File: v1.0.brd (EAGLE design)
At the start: 160 x 100 mm, 19 parts, among them J1 DC-044-A, Q1 IRF520NPBF, U1 MCP23017-E/SO, U2 LM2599T-5.0, U3 74HC139N

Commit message: ADC
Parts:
- added U$1, U$2: MCP3424-E/SL, MCP3424:SOIC127P600X175-14N
- moved C4 2.84 mm to (-142.2, -194.3)
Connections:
- new net N$10: U$1.9
- new net N$11: U$1.10
- new net N$12: U$1.1
- new net N$13: U$1.2
- new net N$14: U$1.3
- new net N$15: U$1.4
- new net N$16: U$1.11
- new net N$8: U$2.9
- new net N$9: U$2.10
- new net VDD: U$1.6, U$2.6
- new net VSS: U$1.5, U$2.5
- net SCL_3V3: now also U$1.8, U$2.8
- net SDA_3V3: now also U$1.7, U$2.7
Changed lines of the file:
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@@
 <attribute name="MPN" value="SS54B" x="-151.13" y="-182.88" size="1.778" layer="27" display="off"/>
 </element>
-<element name="C4" library="Seeed-OPL-2017-01-Capacitor-akita" package="CAP_TH_P35_D80_POL" value="CAP_TH_220UF_25V" x="-144.78" y="-195.58"/>
+<element name="C4" library="Seeed-OPL-2017-01-Capacitor-akita" package="CAP_TH_P35_D80_POL" value="CAP_TH_220UF_25V" x="-142.24" y="-194.31"/>
 <element name="L1" library="inductors" library_urn="urn:adsk.eagle:library:243" package="DR125" value="DR125-330-R 33uH" x="-162.56" y="-193.04"/>
 <element name="USB1" library="Seeed-Connector -2016" package="MICRO-USB5+4P-SMD-0.65-B" value="ST-USB-001G" x="-160.02" y="-205.74">
@@
 <element name="R4" library="Seeed-Resistor-2016" package="R0603" value="100K" x="-181.61" y="-217.17">
 <attribute name="MPN" value="RC0603FR-07100KL" x="-181.61" y="-217.17" size="1.778" layer="27" display="off"/>
+</element>
+<element name="U$1" library="MCP3424" package="SOIC127P600X175-14N" value="MCP3424-E/SL" x="-191.77" y="-212.09">
+<attribute name="MPN" value="MCP3424-E/SL" x="-191.77" y="-212.09" size="1.778" layer="27" display="off"/>
+<attribute name="OC_FARNELL" value="1630424" x="-191.77" y="-212.09" size="1.778" layer="27" display="off"/>
+<attribute name="OC_NEWARK" value="54M4871" x="-191.77" y="-212.09" size="1.778" layer="27" display="off"/>
+<attribute name="PACKAGE" value="SOIC-14" x="-191.77" y="-212.09" size="1.778" layer="27" display="off"/>
+<attribute name="SUPPLIER" value="Microchip" x="-191.77" y="-212.09" size="1.778" layer="27" display="off"/>
+</element>
+<element name="U$2" library="MCP3424" package="SOIC127P600X175-14N" value="MCP3424-E/SL" x="-205.74" y="-212.09">
+<attribute name="MPN" value="MCP3424-E/SL" x="-205.74" y="-212.09" size="1.778" layer="27" display="off"/>
+<attribute name="OC_FARNELL" value="1630424" x="-205.74" y="-212.09" size="1.778" layer="27" display="off"/>
+<attribute name="OC_NEWARK" value="54M4871" x="-205.74" y="-212.09" size="1.778" layer="27" display="off"/>
+<attribute name="PACKAGE" value="SOIC-14" x="-205.74" y="-212.09" size="1.778" layer="27" display="off"/>
+<attribute name="SUPPLIER" value="Microchip" x="-205.74" y="-212.09" size="1.778" layer="27" display="off"/>
 </element>
 </elements>
@@
 <contactref element="U1" pad="12"/>
 <contactref element="PCB1" pad="P$5"/>
+<contactref element="U$1" pad="8"/>
+<contactref element="U$2" pad="8"/>
+<wire x1="-189.4078" y1="-215.9" x2="-203.3778" y2="-215.9" width="0" layer="19" extent="1-1"/>
+<wire x1="-121.3612" y1="24.765" x2="-189.4078" y2="-215.9" width="0" layer="19" extent="1-1"/>
 <wire x1="5.9182" y1="69.1134" x2="-121.3612" y2="24.765" width="0" layer="19" extent="1-1"/>
 </signal>
@@
 <contactref element="U1" pad="13"/>
 <contactref element="PCB1" pad="P$3"/>
+<contactref element="U$1" pad="7"/>
+<contactref element="U$2" pad="7"/>
+<wire x1="-194.1322" y1="-215.9" x2="-208.1022" y2="-215.9" width="0" layer="19" extent="1-1"/>
+<wire x1="-121.3612" y1="23.495" x2="-194.1322" y2="-215.9" width="0" layer="19" extent="1-1"/>
 <wire x1="5.9182" y1="71.6534" x2="-121.3612" y2="23.495" width="0" layer="19" extent="1-1"/>
 </signal>
@@
 <contactref element="R2" pad="1"/>
 <wire x1="-134.62" y1="-181.1475" x2="-87.63" y2="-151.13" width="0" layer="19" extent="1-1"/>
-<wire x1="-143.03" y1="-195.58" x2="-134.62" y2="-181.1475" width="0" layer="19" extent="1-1"/>
-<wire x1="-157.585" y1="-193.04" x2="-143.03" y2="-195.58" width="0" layer="19" extent="1-1"/>
+<wire x1="-140.49" y1="-194.31" x2="-134.62" y2="-181.1475" width="0" layer="19" extent="1-1"/>
+<wire x1="-157.585" y1="-193.04" x2="-140.49" y2="-194.31" width="0" layer="19" extent="1-1"/>
 <wire x1="-171.45" y1="-209.0875" x2="-157.585" y2="-193.04" width="0" layer="19" extent="1-1"/>
 <wire x1="-107.95" y1="-60.7314" x2="-87.63" y2="-151.13" width="0" layer="19" extent="1-1"/>
@@
 <wire x1="-144.78" y1="-184.912" x2="-139.7" y2="-184.912" width="0" layer="19" extent="1-1"/>
 <wire x1="-153.34" y1="-182.88" x2="-144.78" y2="-184.912" width="0" layer="19" extent="1-1"/>
-<wire x1="-146.53" y1="-195.58" x2="-144.78" y2="-184.912" width="0" layer="19" extent="1-1"/>
-<wire x1="-156.62" y1="-206.167" x2="-146.53" y2="-195.58" width="0" layer="19" extent="1-1"/>
+<wire x1="-143.99" y1="-194.31" x2="-144.78" y2="-184.912" width="0" layer="19" extent="1-1"/>
+<wire x1="-156.62" y1="-206.167" x2="-143.99" y2="-194.31" width="0" layer="19" extent="1-1"/>
 <wire x1="-158.72" y1="-205.99" x2="-156.62" y2="-206.167" width="0" layer="19" extent="1-1"/>
 <wire x1="-156.7942" y1="-208.915" x2="-156.62" y2="-206.167" width="0" layer="19" extent="1-1"/>
@@
 <wire x1="-159.37" y1="-205.99" x2="-181.61" y2="-216.408" width="0" layer="19" extent="1-1"/>
 </signal>
+<signal name="VDD">
+<contactref element="U$1" pad="6"/>
+<contactref element="U$2" pad="6"/>
+<wire x1="-194.1322" y1="-214.63" x2="-208.1022" y2="-214.63" width="0" layer="19" extent="1-1"/>
+</signal>
+<signal name="VSS">
+<contactref element="U$1" pad="5"/>
+<contactref element="U$2" pad="5"/>
+<wire x1="-194.1322" y1="-213.36" x2="-208.1022" y2="-213.36" width="0" layer="19" extent="1-1"/>
+</signal>
+<signal name="N$8">
+<contactref element="U$2" pad="9"/>
+</signal>
+<signal name="N$9">
+<contactref element="U$2" pad="10"/>
+</signal>
+<signal name="N$10">
+<contactref element="U$1" pad="9"/>
+</signal>
+<signal name="N$11">
+<contactref element="U$1" pad="10"/>
+</signal>
+<signal name="N$12">
+<contactref element="U$1" pad="1"/>
+</signal>
+<signal name="N$13">
+<contactref element="U$1" pad="2"/>
+</signal>
+<signal name="N$14">
+<contactref element="U$1" pad="3"/>
+</signal>
+<signal name="N$15">
+<contactref element="U$1" pad="4"/>
+</signal>
+<signal name="N$16">
+<contactref element="U$1" pad="11"/>
+</signal>
 </signals>

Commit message: General tidying, PSU mods, and pycom library created and added
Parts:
- removed D3: GREEN-0603, Seeed-LED-2016:LED-0603
- removed Q1: IRF520NPBF, Seeed-Transistor-2016:TO-220
- removed R3: 1K, Seeed-Resistor-2016:R0603
- removed R4: 100K, Seeed-Resistor-2016:R0603
- removed U3: 74HC139N, 74HC139N:DIP254P762X420-16
- removed USB1: ST-USB-001G, Seeed-Connector -2016:MICRO-USB5+4P-SMD-0.65-B
- added C11, C12, C13, C14, C6, C7: 100nf, Seeed-Capacitor-2016:C0603
- added C5, C8: 1UF 6.3V, Seeed-Capacitor-2016:C0402
- added D10, D4, D5, D6, D7, D8, D9: RED-0603, Seeed-LED-2016:LED-0603
- added L2, L3: 330R-1500MA, Seeed-Inductor-2016:L0805
- added R10, R11, R5, R6, R7, R8, R9: 1K, Seeed-Resistor-2016:R0603
- added TP1: PTR1B2,54, testpad:B2,54
- added TP2, TP3: TPB2,54, testpad:B2,54
- added U$3: LOPY, pycom:LOPY
- added U10: 74HC139N, 74HC139N:DIP254P762X420-16
- added USB2: ST-USB-001G, Seeed-Connector -2016:MICRO-USB5+4P-SMD-0.65-B
- R2: value 10K 1/16W -> 100K; device Seeed-Resistor-2016:R0402 -> Seeed-Resistor-2016:R0603
- moved U$1 349.4 mm to (-27.9, 96.5)
- moved U$2 345.9 mm to (-49.5, 96.5)
- moved L1 325.5 mm to (-48.3, 111.8)
- moved C2 315.7 mm to (-62.2, 121.9)
- moved C3 315.7 mm to (-67.3, 121.9)
- moved C4 314.5 mm to (-69.8, 111.8)
- moved C1 306.8 mm to (-27.9, 113.0)
- moved R1 296.9 mm to (-88.9, 111.8)
- moved D2 295.3 mm to (-108.0, 109.2)
- moved D1 277.0 mm to (-100.3, 109.2)
- moved PCB1 176.1 mm to (-100.3, 3.81), flipped to the top, turned to 0 degrees
- moved J1 156.1 mm to (-92.7, 61.0)
- moved U2 134.6 mm to (-74.9, 76.2)
- moved R2 118.0 mm to (-154.9, -92.7)
- moved U1 81.5 mm to (-47.0, 72.4)
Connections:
- removed net N$10: U$1.9
- removed net N$11: U$1.10
- removed net N$5: R4.1, USB1.4
- removed net N$8: U$2.9
- removed net N$9: U$2.10
- removed net VDD: U$1.6, U$2.6
- removed net VSS: U$1.5, U$2.5
- new net +24V: C1.P$P, D1.-, R5.2, U2.1
- new net LOPY_3V3: U$3.P$26
- new net LOPY_P0: U$3.P$2
- new net LOPY_P1: U$3.P$3
- new net LOPY_P10: U$3.P$12
- new net LOPY_P11: U$3.P$13
- new net LOPY_P12: U$3.P$14
- new net LOPY_P13: U$3.P$15
- new net LOPY_P14: U$3.P$16
- new net LOPY_P15: U$3.P$17
- new net LOPY_P16: U$3.P$18
- new net LOPY_P17: U$3.P$19
- new net LOPY_P18: U$3.P$20
- new net LOPY_P19: U$3.P$21
- new net LOPY_P2: U$3.P$4
- new net LOPY_P20: U$3.P$22
- new net LOPY_P21: U$3.P$23
- new net LOPY_P22: U$3.P$24
- new net LOPY_P23: U$3.P$25
- new net LOPY_P3: U$3.P$5
- new net LOPY_P4: U$3.P$6
- new net LOPY_P8: U$3.P$10
- new net LOPY_P9: U$3.P$11
- new net LOPY_RST: U$3.P$1
- new net N$19: C5.1, C7.2, U$2.6
- new net N$22: C14.2, L2.2, TP3.TP
- new net N$23: D10.-, D4.-, D5.-, D6.-, D7.-, D8.-, D9.-
- new net N$28: D10.+, R11.1
- new net N$29: D9.+, R10.1
- new net N$30: D8.+, R9.1
- new net N$31: D7.+, R8.1
- new net N$32: D6.+, R7.1
- new net N$33: D5.+, R6.1
- new net N$34: D4.+, R5.1
- net +3V3: now also C11.2, C12.2, L2.1, TP2.TP
- net +5V: now also C13.2, R6.2, U$3.P$28, U10.16; no longer U3.16
- net +5V/1: now also USB2.1; no longer Q1.3, R3.1, USB1.1
- net +5V_REG_OUT: now also TP1.TP; no longer Q1.1, R2.1
- net GND: now also C1.P$M, C11.1, C12.1, C13.1, C2.2, C3.2, C4.P$P, D2.+, L3.1, U$3.P$27, U10.8, U2.4; no longer U3.8
- net GNDA: now also C14.1, C5.2, C7.1, L3.2, R2.2, U$1.10, U$1.5, U$1.9, U$2.5, U$2.9, USB2.5, USB2.S1, USB2.S2, USB2.S3, USB2.S4, USB2.S5, USB2.S6; no longer C1.P$M, C2.2, C3.2, C4.P$P, D2.+, D3.-, Q1.2, Q1.HEAT, R4.2, U2.4, USB1.5, USB1.S1, USB1.S2, USB1.S3, USB1.S4, USB1.S5, USB1.S6
- net N$1: now also R2.1, USB2.4; no longer D3.+, R3.2
- net N$12: now also C6.2, C8.1, U$1.6; no longer U$1.1
- net N$2: now also C6.1, C8.2; no longer C1.P$P, D1.-, U2.1
- net SPI0_CS0: now also U10.1; no longer U3.1
- net SPI0_CS1: now also U10.15; no longer U3.15

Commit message: seeed dc-dc library finished RTC added
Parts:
- removed C1: CAP_TH_470UF_50V, Seeed-OPL-2017-01-Capacitor-akita:CAP_TH_P50_D100_POL
- removed C3: 100nf, Seeed-Capacitor-2016:C0603
- removed C4: CAP_TH_220UF_25V, Seeed-OPL-2017-01-Capacitor-akita:CAP_TH_P35_D80_POL
- removed D2: 28V-5A, Seeed-Diode-2016:DO-214AA
- removed L1: DR125-330-R 33uH, inductors:DR125
- removed R1: 10K 1/16W, Seeed-Resistor-2016:R0402
- removed TP1: PTR1B2,54, testpad:B2,54
- added BAT1: cr1220, Seeed-Connector -2016:BAT2P-13.5-CR1220
- added TP4: TPB2,54, testpad:B2,54
- added U4: GROVE_DC&DC, seeed_parts:GROVE_DC&DC
- U2: value LM2599T-5.0 -> MCP79412-I/SN; device LM2599T:TO127P470X1016X1740-7P -> imported-parts:SOIC127P600X175-8N
- moved C2 344.2 mm to (-214.6, -186.7)
- moved U2 275.5 mm to (-200.7, -168.9)
- renumbered U$3 to U3
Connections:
- removed net +5V_REG_OUT: C4.P$M, L1.2, R1.1, TP1.TP, U2.6
- removed net N$4: D2.-, L1.1, U2.2
- removed net N$6: C3.1, U2.5
- removed net N$7: R1.2, U2.3
- new net 5V4: R7.2, TP4.TP, U4.P$5, U4.P$6
- net +24V: now also U4.P$1, U4.P$2; no longer C1.P$P, U2.1
- net +3V3: now also C2.2, U2.8
- net GND: now also BAT1.-, C2.1, J1.-, J1.CDN, U4.P$3, U4.P$4, U4.P$7, U4.P$8; no longer C1.P$M, C2.2, C3.2, C4.P$P, D2.+
- net GNDA: no longer J1.-, J1.CDN
- net N$3: now also BAT1.+1, BAT1.+2, U2.3; no longer C2.1, U2.7
- net SCL_3V3: now also U2.6
- net SDA_3V3: now also U2.5

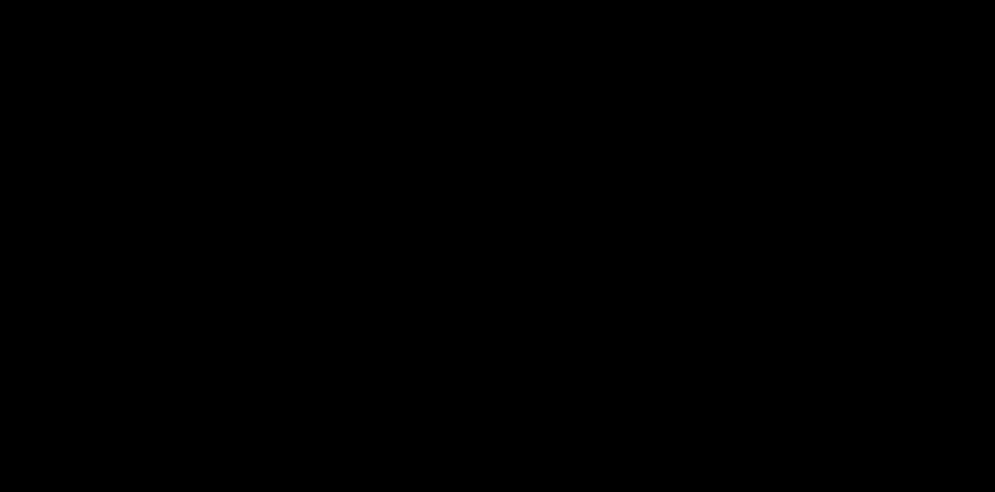
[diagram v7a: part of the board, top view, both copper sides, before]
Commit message: added crystal for RTC
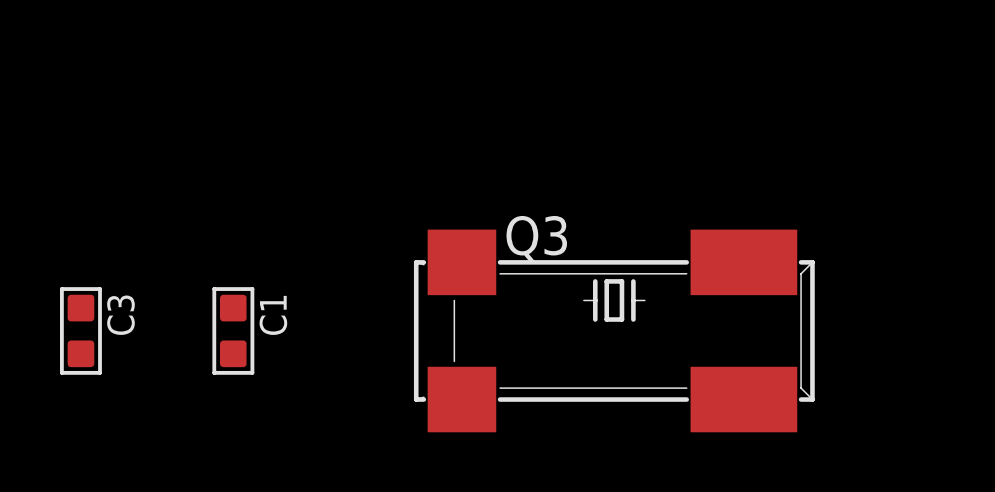
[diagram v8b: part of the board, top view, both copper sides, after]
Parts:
- added C1, C3: 100nf, Seeed-Capacitor:C0603
- added Q3: 6pF@32.7680kHz, crystal:86SMX
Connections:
- new net X1_RTC: C1.1, Q3.4, U2.1
- new net X2_RTC: C3.1, Q3.1, U2.2
- net GND: now also C1.2, C3.2
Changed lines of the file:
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@@
 <attribute name="MPN" value="CC0603KRX7R9BB104" x="-214.63" y="-186.69" size="1.778" layer="27" display="off"/>
+</element>
+<element name="Q3" library="crystal" package="86SMX" value="6pF@32.7680kHz" x="-207.01" y="-213.36"/>
+<element name="C1" library="Seeed-Capacitor" library_urn="urn:adsk.eagle:library:464" package="C0603" value="100nf" x="-219.71" y="-213.36">
+<attribute name="MPN" value="CC0603KRX7R9BB104" x="-219.71" y="-213.36" size="1.778" layer="27" display="off"/>
+</element>
+<element name="C3" library="Seeed-Capacitor" library_urn="urn:adsk.eagle:library:464" package="C0603" value="100nf" x="-224.79" y="-213.36">
+<attribute name="MPN" value="CC0603KRX7R9BB104" x="-224.79" y="-213.36" size="1.778" layer="27" display="off"/>
 </element>
 </elements>
@@
 <contactref element="C2" pad="1"/>
 <contactref element="BAT1" pad="-"/>
+<contactref element="C1" pad="2"/>
+<contactref element="C3" pad="2"/>
 <wire x1="-164.719" y1="-102.87" x2="-160.02" y2="-90.678" width="0" layer="19" extent="1-1"/>
 <wire x1="-148.59" y1="-68.58" x2="-160.02" y2="-90.678" width="0" layer="19" extent="1-1"/>
@@
 <wire x1="-196.85" y1="-182.88" x2="-203.0222" y2="-170.815" width="0" layer="19" extent="1-1"/>
 <wire x1="-214.63" y1="-185.928" x2="-196.85" y2="-182.88" width="0" layer="19" extent="1-1"/>
+<wire x1="-219.71" y1="-214.122" x2="-214.63" y2="-185.928" width="0" layer="19" extent="1-1"/>
+<wire x1="-224.79" y1="-214.122" x2="-219.71" y2="-214.122" width="0" layer="19" extent="1-1"/>
 <wire x1="-114.3" y1="4.572" x2="-129.54" y2="-43.688" width="0" layer="19" extent="1-1"/>
 <wire x1="-86.8934" y1="57.5818" x2="-114.3" y2="4.572" width="0" layer="19" extent="1-1"/>
@@
 <wire x1="-190.119" y1="-182.88" x2="-203.581" y2="-182.88" width="0" layer="19" extent="1-1"/>
 </signal>
+<signal name="X1_RTC">
+<contactref element="U2" pad="1"/>
+<contactref element="Q3" pad="4"/>
+<contactref element="C1" pad="1"/>
+<wire x1="-212.09" y1="-211.074" x2="-219.71" y2="-212.598" width="0" layer="19" extent="1-1"/>
+<wire x1="-203.0222" y1="-167.005" x2="-212.09" y2="-211.074" width="0" layer="19" extent="1-1"/>
+</signal>
+<signal name="X2_RTC">
+<contactref element="U2" pad="2"/>
+<contactref element="Q3" pad="1"/>
+<contactref element="C3" pad="1"/>
+<wire x1="-212.09" y1="-215.646" x2="-224.79" y2="-212.598" width="0" layer="19" extent="1-1"/>
+<wire x1="-203.0222" y1="-168.275" x2="-212.09" y2="-215.646" width="0" layer="19" extent="1-1"/>
+</signal>
 </signals>
